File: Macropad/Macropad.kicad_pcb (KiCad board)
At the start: 2 copper layers, 112.2 x 163 mm, 115 parts, among them J201 TSOP4838_C124647, J202 IR_LED_TX_HDR, J301 LED_CHAIN, J302 LCD_SPI_PWRDATA, J303 LCD_SPI_CTRL, J304 TOUCH_I2C_SD, J400 BATTERY_LIPO, J401 BAT_CHG_BOOST, J402 USB_C_CHG_IN, Q501 AO3400A, SW1 SW_Push, SW10 SW_Push, SW11 SW_Push, SW12 SW_Push, SW13 SW_Push, SW14 SW_Push, SW15 SW_Push, SW16 SW_Push, SW17 SW_Push, SW18 SW_Push, SW19 SW_Push, SW2 SW_Push, SW20 SW_Push, SW21 SW_Push, SW22 SW_Push, SW23 SW_Push, SW24 SW_Push, SW25 SW_Push, SW26 SW_Push, SW3 SW_Push, SW4 SW_Push, SW401 RotaryEncoder_Switch, SW402 SW_Push, SW5 SW_Push, SW6 SW_Push, SW7 SW_Push, SW8 SW_Push, SW9 SW_Push, U402 AMS1117-3.3, U403 MCP73831, U404 MT3608, U901 ESP32-S3-WROOM-1-N8R8

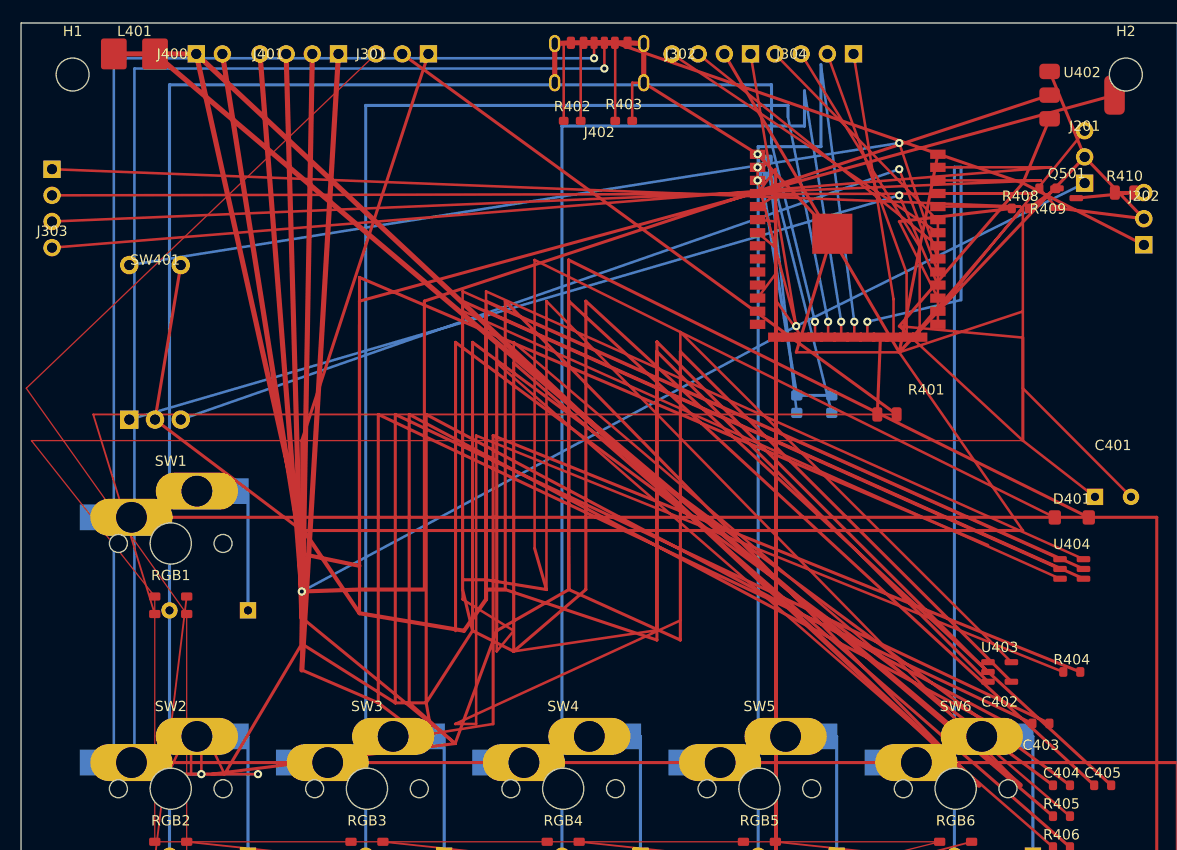
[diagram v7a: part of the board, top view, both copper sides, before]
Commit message: Finalize macropad firmware + schematic/pcb validation updates
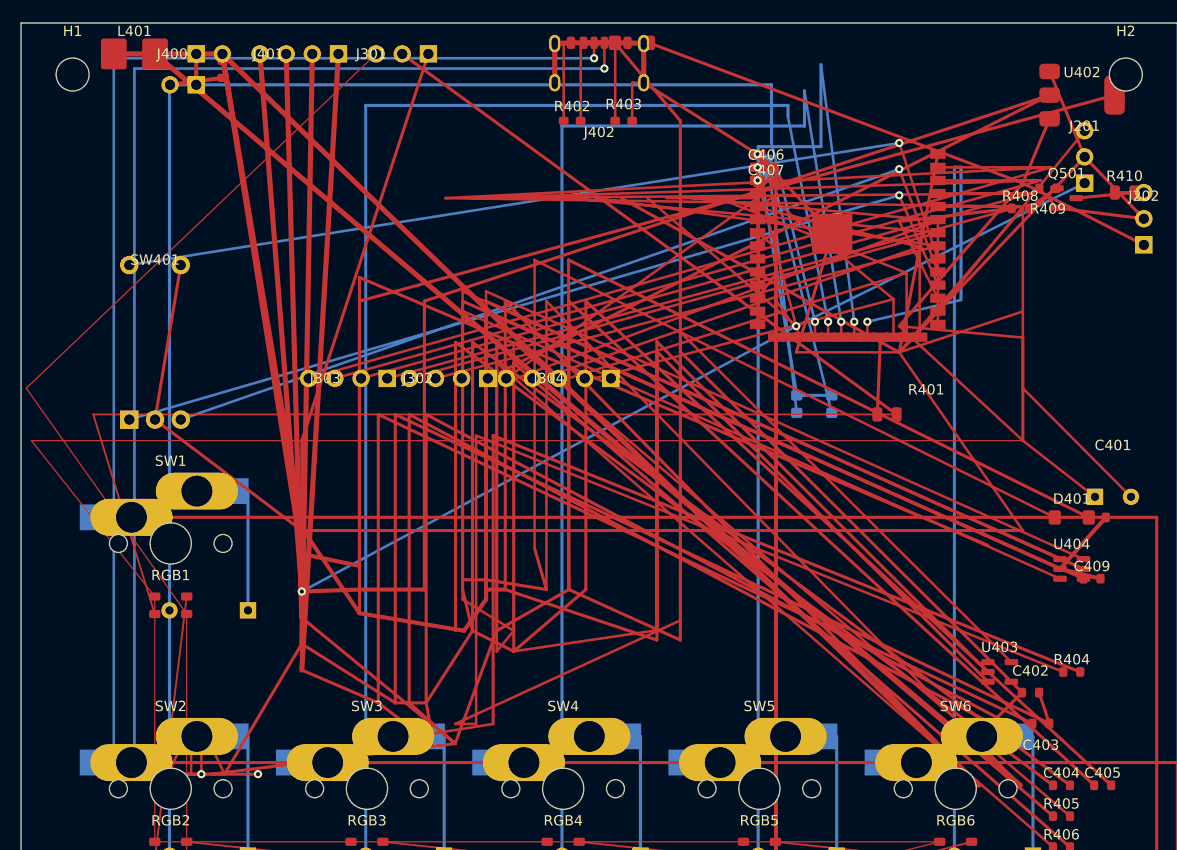
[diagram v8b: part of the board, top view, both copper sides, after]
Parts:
- added C406: 100nF, C_0603_1608Metric_LOCAL, F.Cu at (67.3, -27.0)
- added C407: 22uF, C_0603_1608Metric_LOCAL, F.Cu at (67.3, -25.5)
- added C408: 10uF, C_0603_1608Metric_LOCAL, F.Cu at (99.5, 7.00)
- added C409: 10uF, C_0603_1608Metric_LOCAL, F.Cu at (99.0, 12.9)
- added D402: SS14_VBUS_TO_5VSYS, D_SOD123_LOCAL, F.Cu at (54.3, -39.1)
- added F401: PTC_0.5A, R_0603_1608Metric_LOCAL, F.Cu at (14.5, -36.5)
- added JP403: SHIP_JUMPER, GEN_PinHeader_1x2_P2.54, F.Cu at (12.0, -35.0)
- J303: footprint GEN_PinHeader_1x4_P2.54 -> GEN_PinHeader_1x5_P2.54
- J304: value TOUCH_I2C_SD -> TOUCH_I2C_SD_IRQ; footprint GEN_PinHeader_1x4_P2.54 -> GEN_PinHeader_1x5_P2.54
- U402: value AMS1117-3.3 -> AP7361C-33E
- moved J302 40.5 mm to (36.5, -6.50)
- moved J304 39.3 mm to (48.5, -6.50)
- moved J303 33.1 mm to (26.7, -6.50), turned to 90 degrees
- moved C402 4.24 mm to (93.0, 24.0)
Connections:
- C401 pad 1: 5V -> 5V_SYS
- C402 pad 1: 5V -> 5V_SYS
- C405 pad 1: 5V -> 5V_SYS
- D401 pad 2: 5V -> 5V_SYS
- J202 pad 1: 5V -> 5V_SYS
- J301 pad 1: 5V -> 5V_SYS
- J400 pad 1: BAT+ -> BAT_RAW
- J401 pad 3: 5V -> 5V_SYS
- J402 pad A9: 5V -> VBUS
- J402 pad B9: 5V -> VBUS
- R405 pad 1: 5V -> 5V_SYS
- RGB1 pad 1: 5V -> 5V_SYS
- RGB10 pad 1: 5V -> 5V_SYS
- RGB11 pad 1: 5V -> 5V_SYS
- RGB12 pad 1: 5V -> 5V_SYS
- RGB13 pad 1: 5V -> 5V_SYS
- RGB14 pad 1: 5V -> 5V_SYS
- RGB15 pad 1: 5V -> 5V_SYS
- RGB16 pad 1: 5V -> 5V_SYS
- RGB17 pad 1: 5V -> 5V_SYS
- RGB18 pad 1: 5V -> 5V_SYS
- RGB19 pad 1: 5V -> 5V_SYS
- RGB2 pad 1: 5V -> 5V_SYS
- RGB20 pad 1: 5V -> 5V_SYS
- RGB21 pad 1: 5V -> 5V_SYS
- RGB22 pad 1: 5V -> 5V_SYS
- RGB23 pad 1: 5V -> 5V_SYS
- RGB24 pad 1: 5V -> 5V_SYS
- RGB25 pad 1: 5V -> 5V_SYS
- RGB26 pad 1: 5V -> 5V_SYS
- RGB3 pad 1: 5V -> 5V_SYS
- RGB4 pad 1: 5V -> 5V_SYS
- RGB5 pad 1: 5V -> 5V_SYS
- RGB6 pad 1: 5V -> 5V_SYS
- RGB7 pad 1: 5V -> 5V_SYS
- RGB8 pad 1: 5V -> 5V_SYS
- RGB9 pad 1: 5V -> 5V_SYS
- U402 pad 3: 5V -> 5V_SYS
- U403 pad 4: 5V -> VBUS
- U901 pad 14: (no net) -> TOUCH_INT
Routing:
- net 5V: track 1607.1 -> 0.00 mm
- net 5V_SYS: track 0.00 -> 1533.3 mm
- net VBUS: track 0.00 -> 108.7 mm
- net LCD_SCLK: track 31.1 -> 89.2 mm
- net LCD_MOSI: track 29.8 -> 84.0 mm
- net 3V3: track 391.2 -> 444.7 mm
- net TOUCH_INT: track 0.00 -> 51.1 mm
- net SD_CS: track 32.7 -> 77.7 mm
- net TOUCH_SCL: track 30.8 -> 67.7 mm
- net LCD_BL: track 108.3 -> 144.8 mm
- net SPI_MISO: track 28.8 -> 60.3 mm
- net LCD_RST: track 106.1 -> 136.5 mm
- net LCD_DC: track 104.0 -> 130.7 mm
- net LCD_CS: track 102.1 -> 127.5 mm
- net TOUCH_SDA: track 27.8 -> 49.1 mm
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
